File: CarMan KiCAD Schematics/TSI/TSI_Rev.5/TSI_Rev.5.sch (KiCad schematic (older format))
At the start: 33 parts, among them J1 TSV, J10 Breakered GLV, J11 Dashboard/EPAL, J12 Battery Packs SL, J13 RSP Safety Loop, J14.1 Logic Conn. 1, J14.2 Logic Conn. 2, J15 Roll Hoop TSAL, J16 Throttle Plau., J17 Brakes & BOT SL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

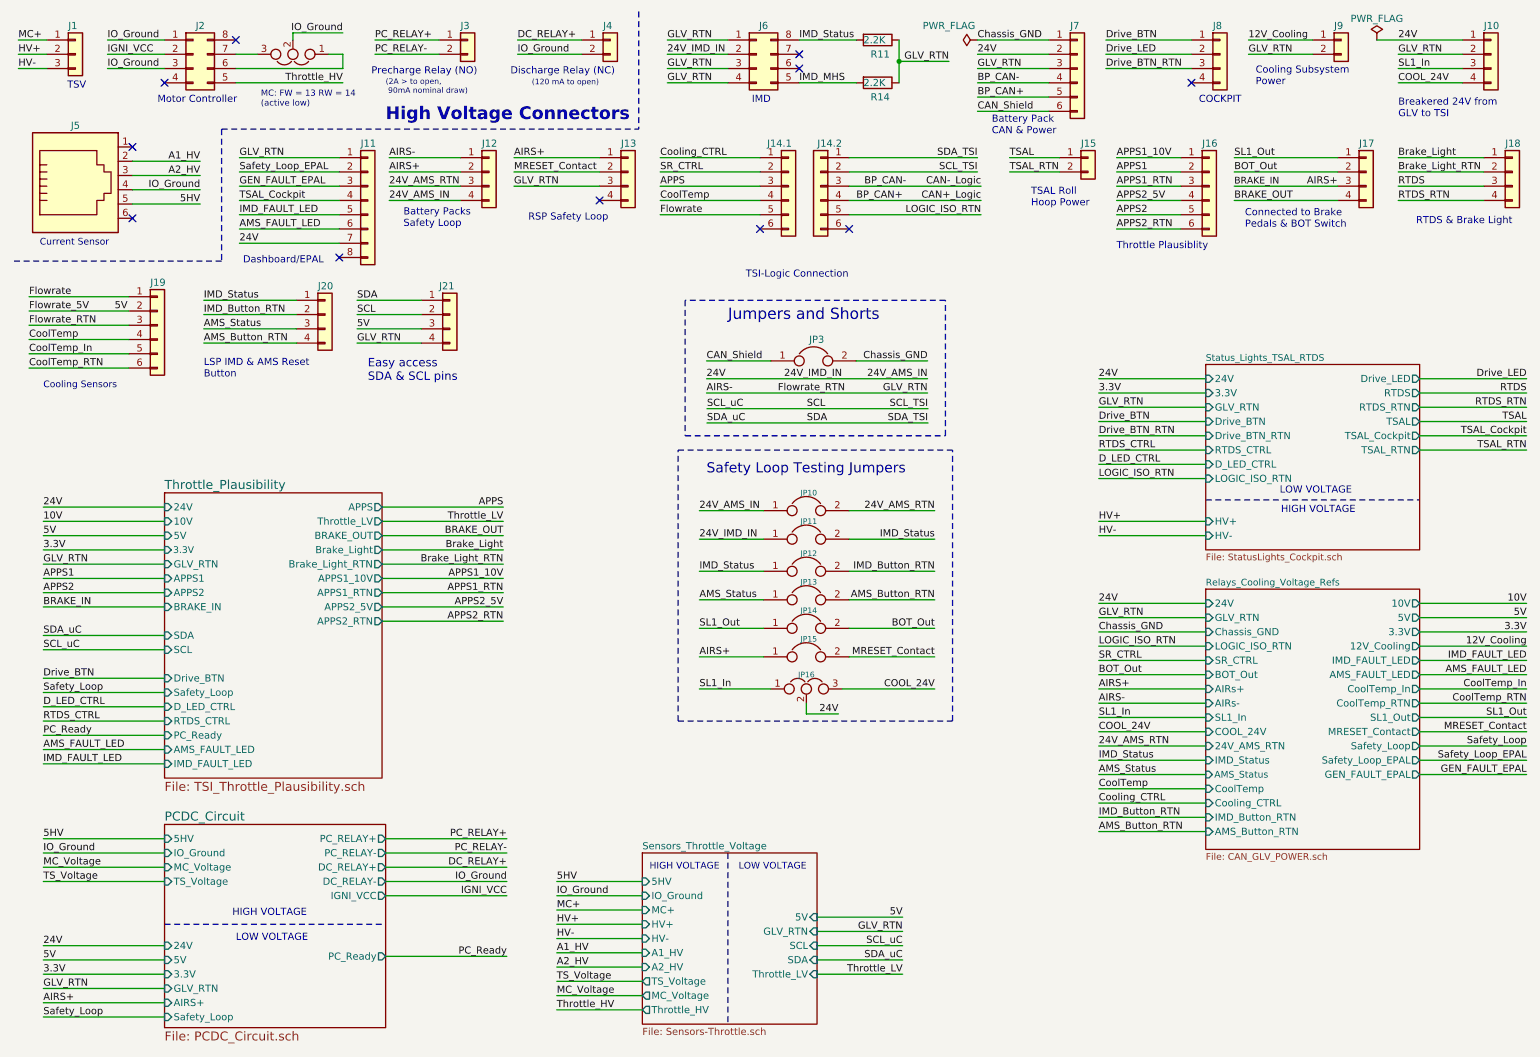
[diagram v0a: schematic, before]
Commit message: - Added SDA & SCL pull-up resistors (to 5V) - Confirmed that all inputs to the GPIO is 5V - Eliminated redundancy of SDA & SCL signals, one signal pervades through whole TSI board and is shorted to SDA_TSI_GLV & SCL_TSI_GLV
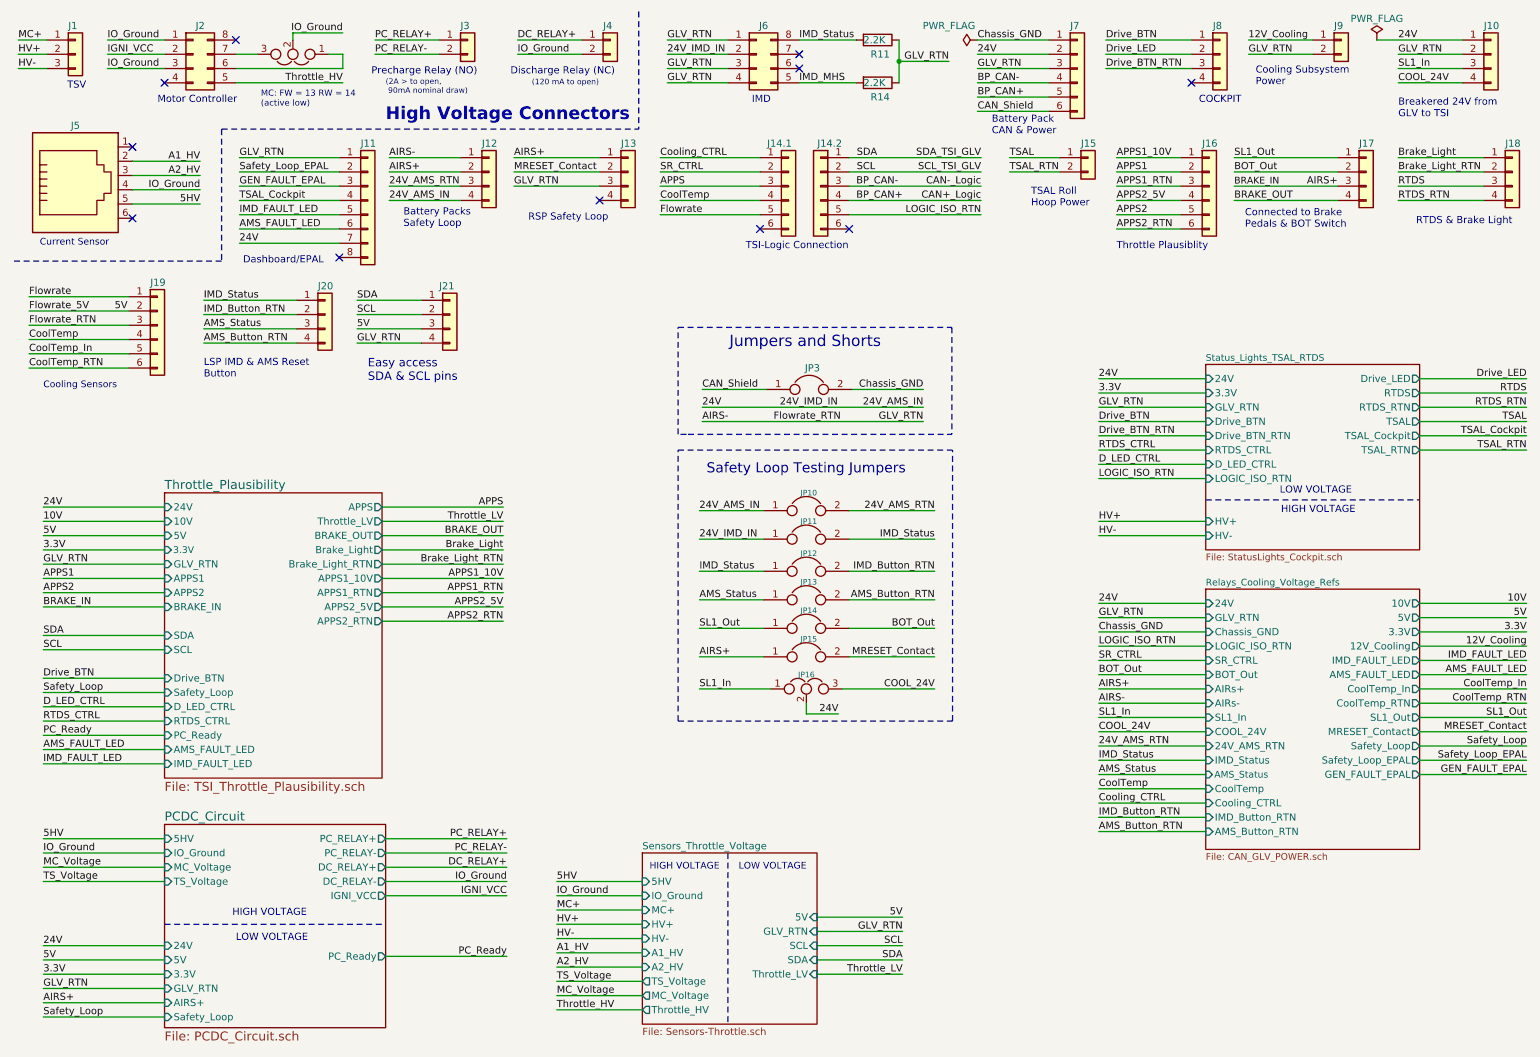
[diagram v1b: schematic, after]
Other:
- moved on the sheet: JP3
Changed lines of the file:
@@
 5V
 Text Label 700  4850 0    50   ~ 0
-SDA_uC
+SDA
 Text Label 700  4950 0    50   ~ 0
-SCL_uC
+SCL
 Text Label 6725 6825 2    50   ~ 0
 5V
@@
 Text Label 8100 5325 0    50   ~ 0
 AIRS-
-Text Label 7250 1600 2    50   ~ 0
-SCL_TSI
-Text Label 7250 1500 2    50   ~ 0
-SDA_TSI
+Text Label 7275 1600 2    50   ~ 0
+SCL_TSI_GLV
+Text Label 7275 1500 2    50   ~ 0
+SDA_TSI_GLV
 Text Label 5025 1500 0    50   ~ 0
 Cooling_CTRL
@@
 Text Label 11100 3350 2    50   ~ 0
 TSAL
-Text Notes 5625 2350 0    50   ~ 0
+Text Notes 5625 2150 0    50   ~ 0
 TSI-Logic Connection\n
 Text Label 7250 1075 0    50   ~ 0
@@
 	4300 7375 4900 7375
 Text Label 6725 7025 2    50   ~ 0
-SCL_uC
+SCL
 Text Label 6725 7125 2    50   ~ 0
-SDA_uC
+SDA
 Wire Wire Line
 	7250 775  7750 775
@@
 Text Label 8100 3750 0    49   ~ 0
 LOGIC_ISO_RTN
-Text Label 5850 3150 0    50   ~ 0
+Text Label 5820 3350 0    50   ~ 0
 Flowrate_RTN
 Wire Wire Line
-	5353 3260 6903 3260
-Text Label 5353 3260 0    50   ~ 0
-SCL_uC
-Text Label 6903 3260 2    50   ~ 0
-SCL_TSI
-Text Label 6053 3260 0    50   ~ 0
-SCL
-Wire Wire Line
-	5353 3360 6903 3360
-Text Label 5353 3360 0    50   ~ 0
-SDA_uC
-Text Label 6053 3360 0    50   ~ 0
-SDA
-Text Label 6903 3360 2    50   ~ 0
-SDA_TSI
-Wire Wire Line
-	5350 3150 6900 3150
-Text Label 5350 3150 0    50   ~ 0
+	5320 3350 6870 3350
+Text Label 5320 3350 0    50   ~ 0
 AIRS-
-Text Label 6900 3150 2    50   ~ 0
+Text Label 6870 3350 2    50   ~ 0
 GLV_RTN
-Text Label 5350 3050 0    50   ~ 0
+Text Label 5320 3250 0    50   ~ 0
 24V
-Text Label 6900 3050 2    50   ~ 0
+Text Label 6870 3250 2    50   ~ 0
 24V_AMS_IN
 Wire Wire Line
-	5350 3050 6900 3050
-Text Label 6300 3050 2    50   ~ 0
+	5320 3250 6870 3250
+Text Label 6270 3250 2    50   ~ 0
 24V_IMD_IN
 Wire Wire Line
-	5350 2925 5800 2925
-Wire Wire Line
-	6900 2925 6400 2925
-Text Label 6900 2925 2    50   ~ 0
+	5320 3125 5770 3125
+Wire Wire Line
+	6870 3125 6370 3125
+Text Label 6870 3125 2    50   ~ 0
 Chassis_GND
-Text Label 5350 2925 0    50   ~ 0
+Text Label 5320 3125 0    50   ~ 0
 CAN_Shield
 $Comp
 L Device:Jumper JP?
 U 1 1 601967AD
-P 6100 2925
+P 6070 3125
 AR Path="/6196BF15/601967AD" Ref="JP?"  Part="1"
 AR Path="/601967AD" Ref="JP3"  Part="1"
-F 0 "JP3" H 6175 3075 50  0000 R CNN
-F 1 "If CAN_Shield & Chassis_GND need to be shorted together, weren't sure" H 6800 2925 50  0001 R CNN
-F 2 "Connector_PinHeader_2.54mm:PinHeader_1x02_P2.54mm_Vertical" H 6100 2925 50  0001 C CNN
-F 3 "~" H 6100 2925 50  0001 C CNN
-	1    6100 2925
+F 0 "JP3" H 6145 3275 50  0000 R CNN
+F 1 "If CAN_Shield & Chassis_GND need to be shorted together, weren't sure" H 6770 3125 50  0001 R CNN
+F 2 "Connector_PinHeader_2.54mm:PinHeader_1x02_P2.54mm_Vertical" H 6070 3125 50  0001 C CNN
+F 3 "~" H 6070 3125 50  0001 C CNN
+	1    6070 3125
 	1    0    0    -1
 $EndComp
@@
 Wire Notes Line
 	4875 475  4875 1300
-Text Label 6750 1700 2    50   ~ 0
+Text Label 6400 1700 0    50   ~ 0
 BP_CAN-
 Text Label 6400 1800 0    50   ~ 0
@@
 Text Notes 2225 1150 0    43   ~ 0
 MC: FW = 13 RW = 14\n(active low)
-Text Notes 5500 2650 0    79   ~ 0
+Text Notes 5510 2840 0    79   ~ 0
 Jumpers and Shorts
-Wire Notes Line
-	7025 2500 5200 2500
 Text Notes 2050 7000 0    50   ~ 0
 LOW VOLTAGE\n
@@
 Text Label 6950 5225 2    49   ~ 0
 COOL_24V
-Wire Notes Line
-	7025 3450 7025 2500
-Wire Notes Line
-	5200 2500 5200 3450
-Wire Notes Line
-	5200 3450 7025 3450
 $Comp
 L Device:Jumper JP?
@@
 APPS
 Wire Wire Line
-	6350 1500 7250 1500
-Wire Wire Line
-	6350 1600 7250 1600
-Wire Wire Line
 	6350 1900 7275 1900
 NoConn ~ 5725 2000
 NoConn ~ 6350 2000
+Text Label 6403 1600 0    50   ~ 0
+SCL
+Text Label 6403 1500 0    50   ~ 0
+SDA
+Wire Notes Line
+	7070 2690 7070 3440
+Wire Notes Line
+	5220 3440 7070 3440
+Wire Notes Line
+	5210 3440 5150 3440
+Wire Notes Line
+	5150 3440 5150 2690
+Wire Notes Line
+	5150 2690 7070 2690
+Wire Wire Line
+	6350 1600 7275 1600
+Wire Wire Line
+	6350 1500 7275 1500
 $EndSCHEMATC

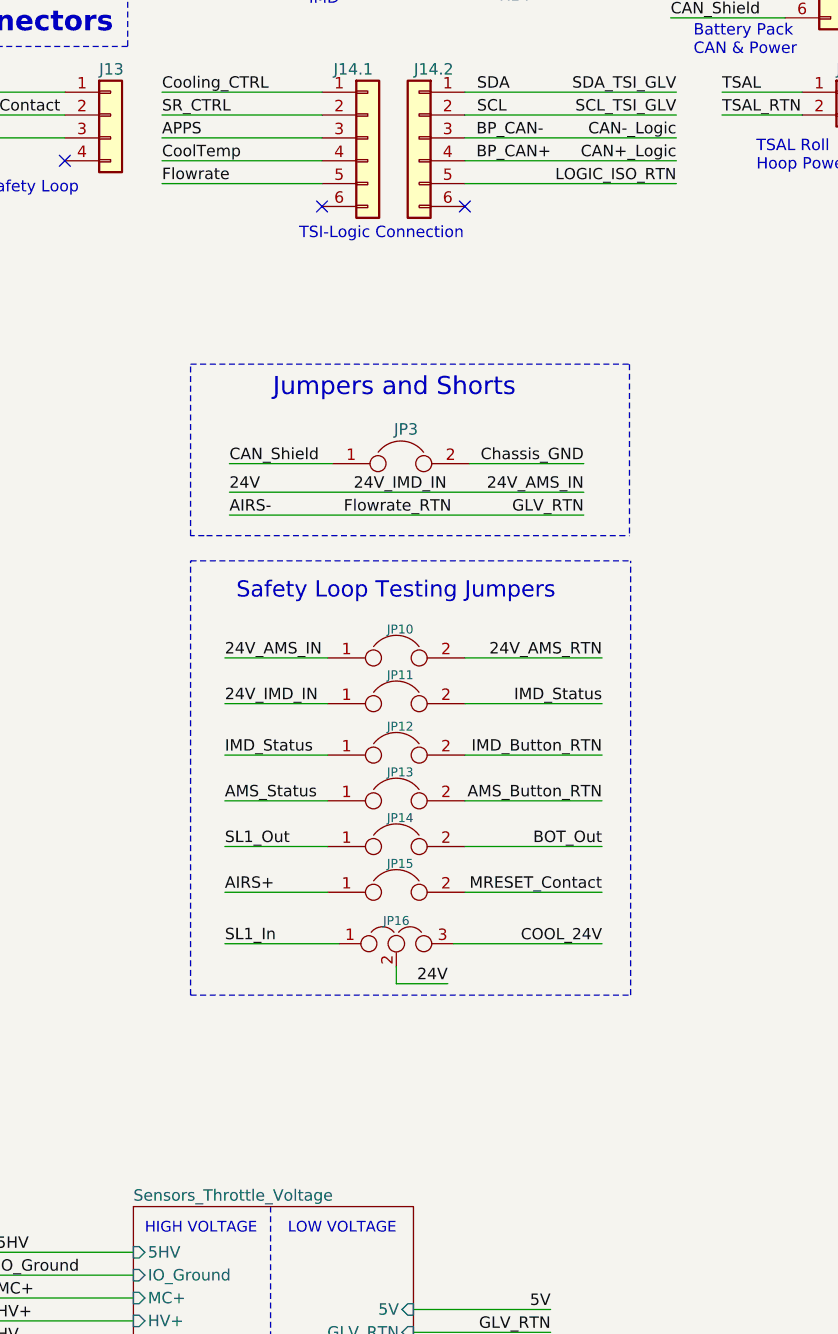
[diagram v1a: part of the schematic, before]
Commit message: Added isolation and state LEDS
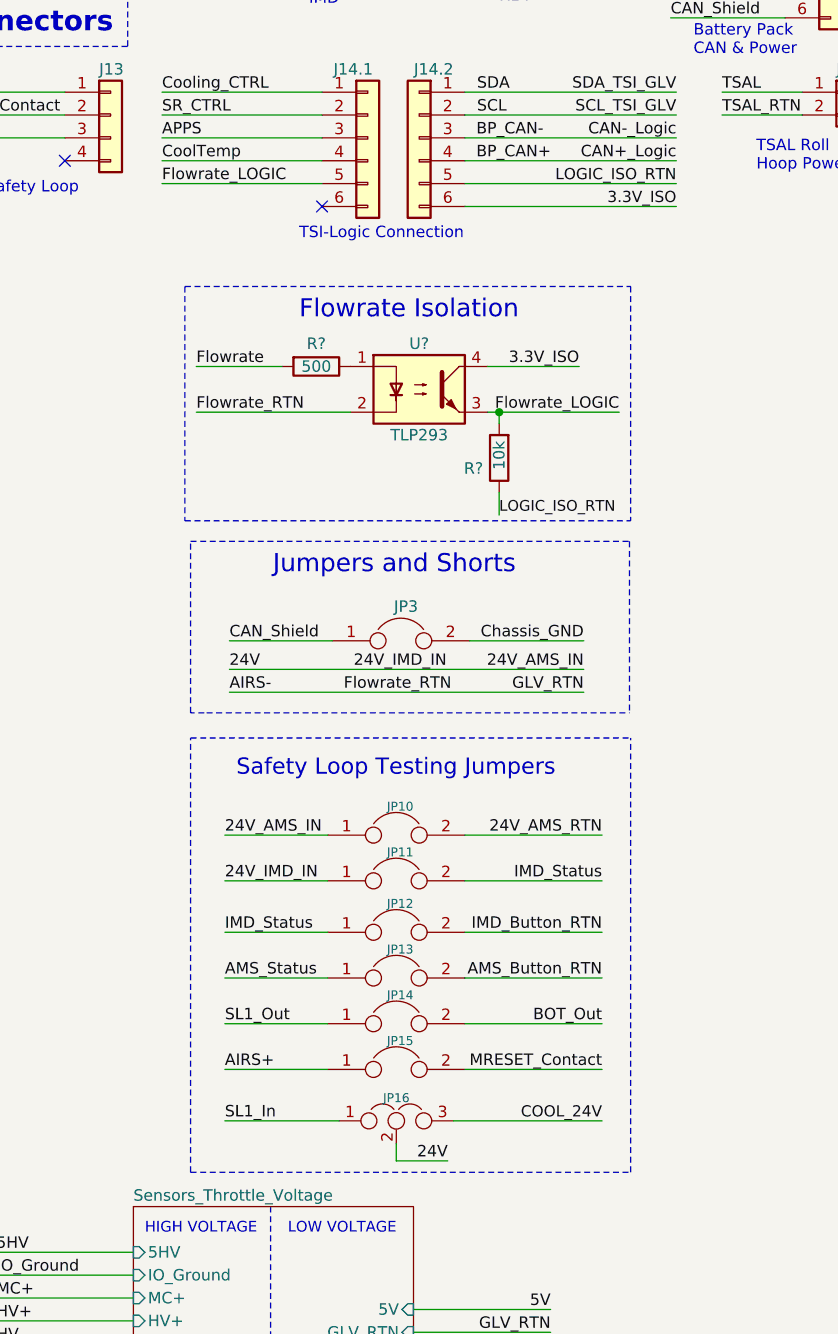
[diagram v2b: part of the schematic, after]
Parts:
- added R?: 500, Resistor_SMD:R_0805_2012Metric_Pad1.15x1.40mm_HandSolder, symbol Device:R
- added R?: 10k, Resistor_SMD:R_0805_2012Metric_Pad1.15x1.40mm_HandSolder, symbol Device:R
- added U?: TLP293, Package_SO:SOIC-4_4.55x2.6mm_P1.27mm, symbol TSI_Rev.5-rescue:TLP293-CarMan_KiCAD_Library-TSI_Rev.5-rescue
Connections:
- net AIRS-: now also U?.2
- net Flowrate: now also R?.2; no longer J14.1.5 (Pin_5)
- net LOGIC_ISO_RTN: now also R?.1
- net 3.3V_ISO: now reaches J14.2.6 (Pin_6)
- net 3.3V_ISO: now also U?.4
- new net: R?.1, U?.1
- new net Flowrate_LOGIC: J14.1.5 (Pin_5), R?.2, U?.3
- no-connect marks 11 -> 10
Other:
- note added: "Flowrate Isolation"
- moved on the sheet: JP10, JP11, JP12, JP13, JP14, JP15, JP16, JP3

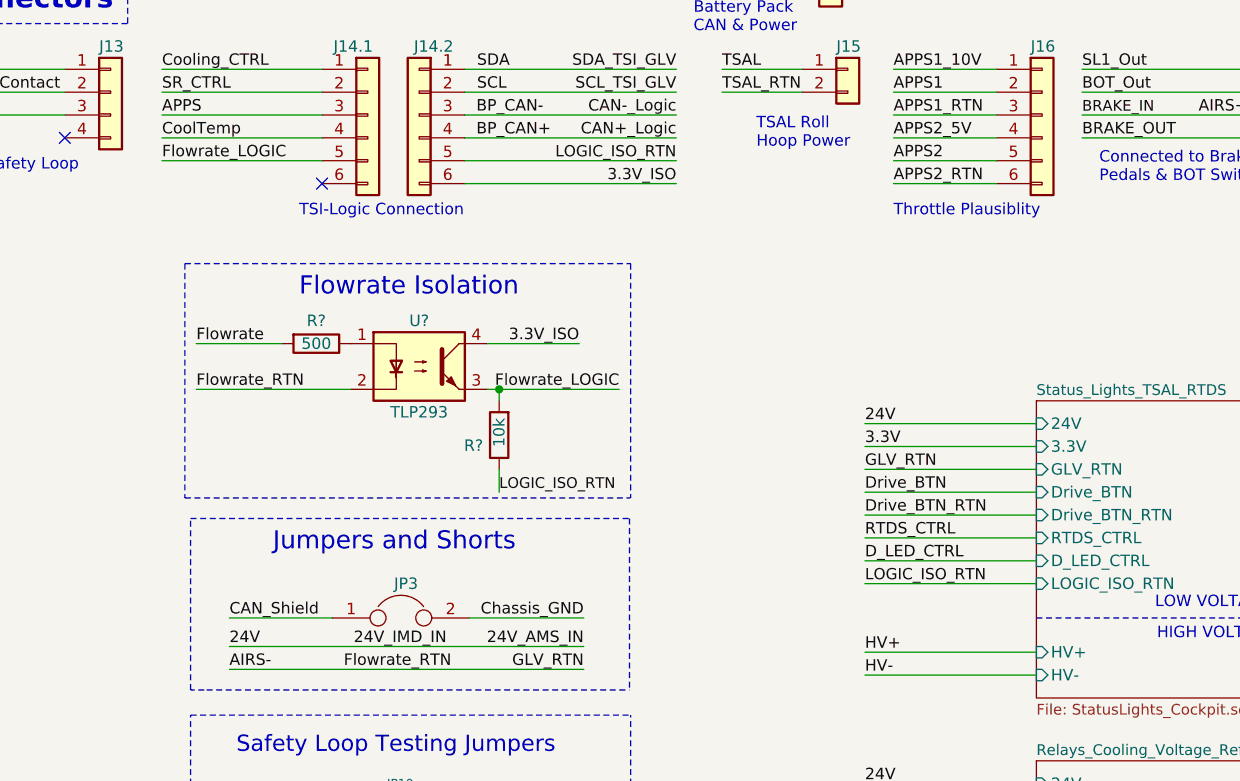
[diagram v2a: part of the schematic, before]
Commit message: Redid PCB added new cooling converter footprint and symbol
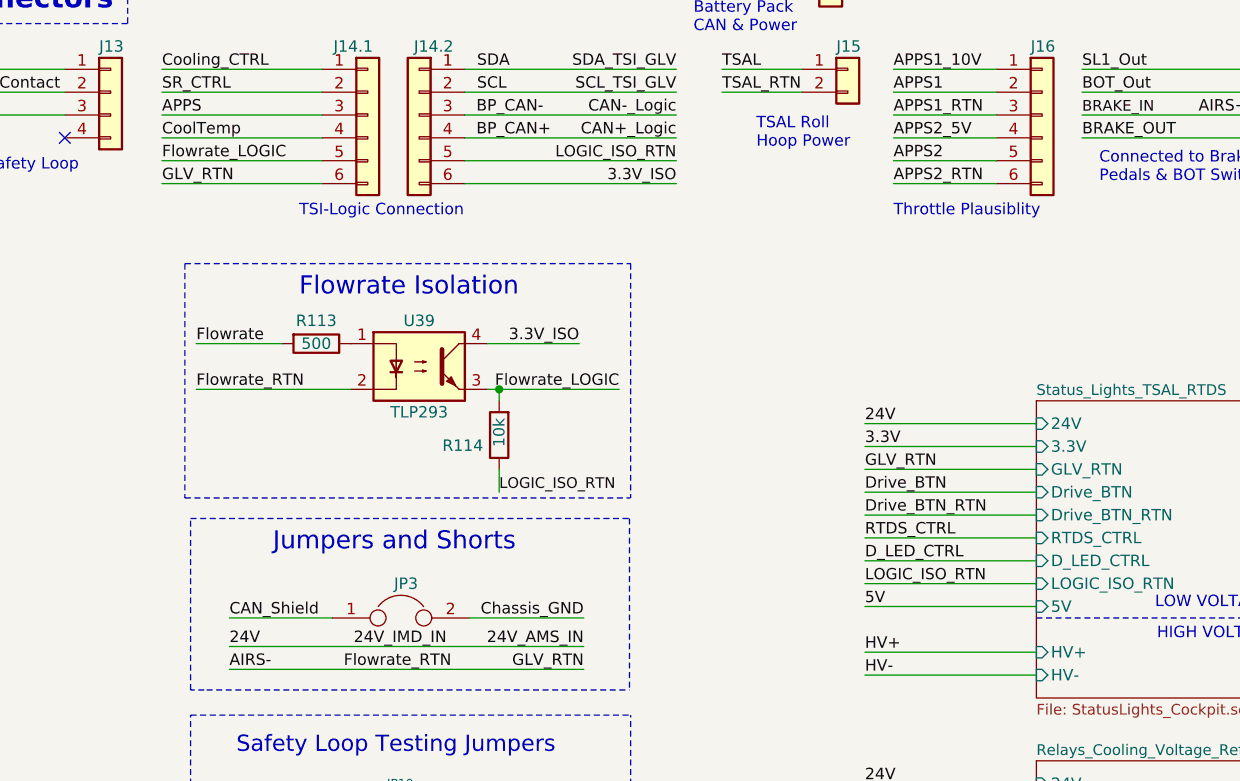
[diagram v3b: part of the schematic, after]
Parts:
- gave numbers to parts that had none: 3
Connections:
- net AIRS-: now also J14.1.6 (Pin_6)
- no-connect marks 10 -> 9
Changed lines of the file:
@@
 F16 "Drive_LED" O R 10350 3050 50
 F17 "LOGIC_ISO_RTN" I L 8850 3750 50
+F18 "5V" I L 8850 3850 50
 $EndSheet
 $Sheet
@@
 Wire Wire Line
 	6350 1900 7275 1900
-NoConn ~ 5725 2000
 Text Label 6403 1600 0    50   ~ 0
 SCL
@@
 P 5700 2700
 AR Path="/5FE1DE7D/60821220" Ref="R?"  Part="1"
-AR Path="/60821220" Ref="R?"  Part="1"
-F 0 "R?" V 5600 2700 50  0000 C CNN
+AR Path="/60821220" Ref="R113"  Part="1"
+F 0 "R113" V 5600 2700 50  0000 C CNN
 F 1 "500" V 5700 2700 50  0000 C CNN
 F 2 "Resistor_SMD:R_0805_2012Metric_Pad1.15x1.40mm_HandSolder" V 5630 2700 50  0001 C CNN
@@
 Flowrate
 $Comp
-L TSI_Rev.5-rescue:TLP293-CarMan_KiCAD_Library-TSI_Rev.5-rescue U?
+L TSI_Rev.5-rescue:TLP293-CarMan_KiCAD_Library-TSI_Rev.5-rescue U39
 U 1 1 60821228
 P 6150 2800
-F 0 "U?" H 6150 3000 50  0000 C CNN
+F 0 "U39" H 6150 3000 50  0000 C CNN
 F 1 "TLP293" H 6150 2600 50  0000 C CNN
 F 2 "Package_SO:SOIC-4_4.55x2.6mm_P1.27mm" H 5950 2600 50  0001 L CIN
@@
 P 6500 3100
 AR Path="/5FE1DE7D/60821231" Ref="R?"  Part="1"
-AR Path="/60821231" Ref="R?"  Part="1"
-F 0 "R?" H 6570 3146 50  0000 L CNN
+AR Path="/60821231" Ref="R114"  Part="1"
+F 0 "R114" H 6570 3146 50  0000 L CNN
 F 1 "10k" V 6500 3025 50  0000 L CNN
 F 2 "Resistor_SMD:R_0805_2012Metric_Pad1.15x1.40mm_HandSolder" V 6430 3100 50  0001 C CNN
@@
 Wire Notes Line
 	5125 2350 7075 2350
+Wire Wire Line
+	5025 2000 5725 2000
+Text Label 5025 2000 0    50   ~ 0
+GLV_RTN
+Wire Wire Line
+	8100 3850 8850 3850
+Text Label 8100 3850 0    49   ~ 0
+5V
 $EndSCHEMATC
